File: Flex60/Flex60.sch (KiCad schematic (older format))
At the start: 128 parts, among them SW1 RESET, U1 ATmega32U4-AU, Y1 16MHz

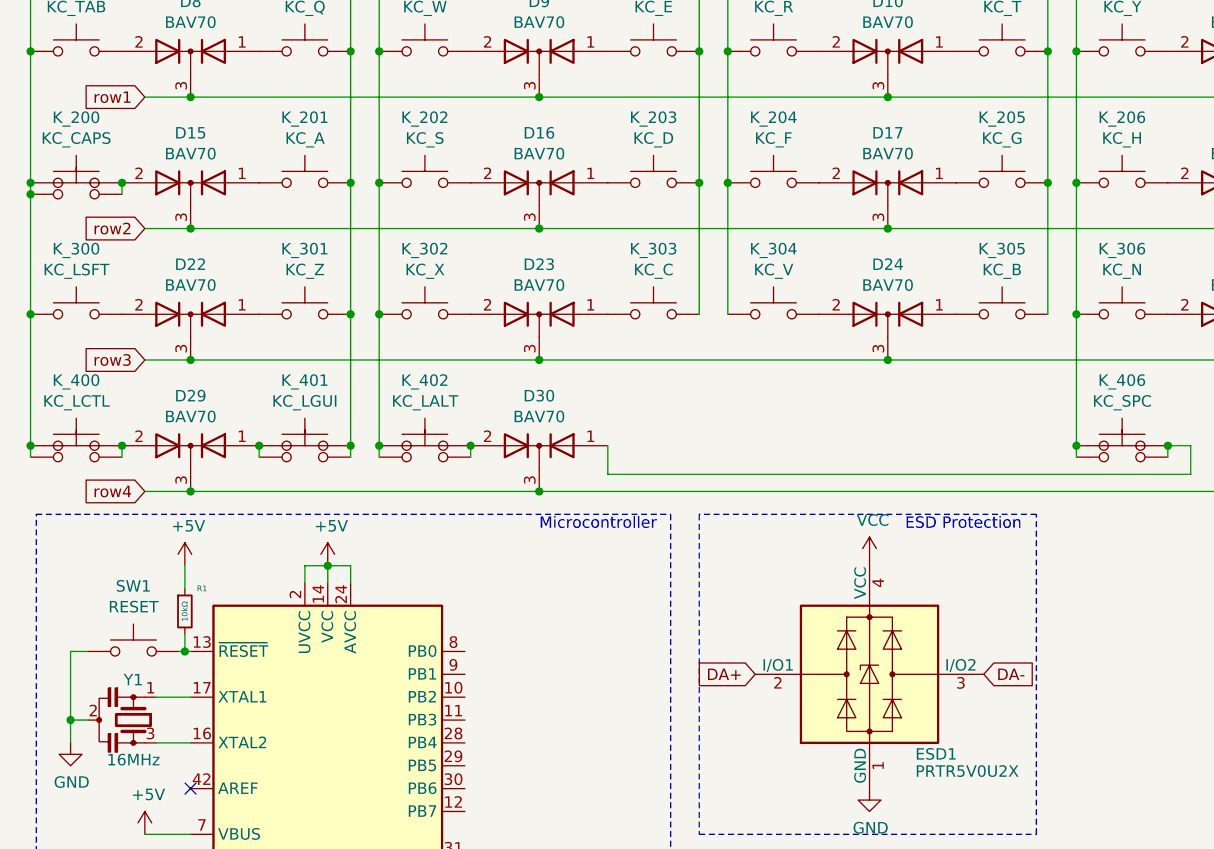
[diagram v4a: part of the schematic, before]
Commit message: MCU placement
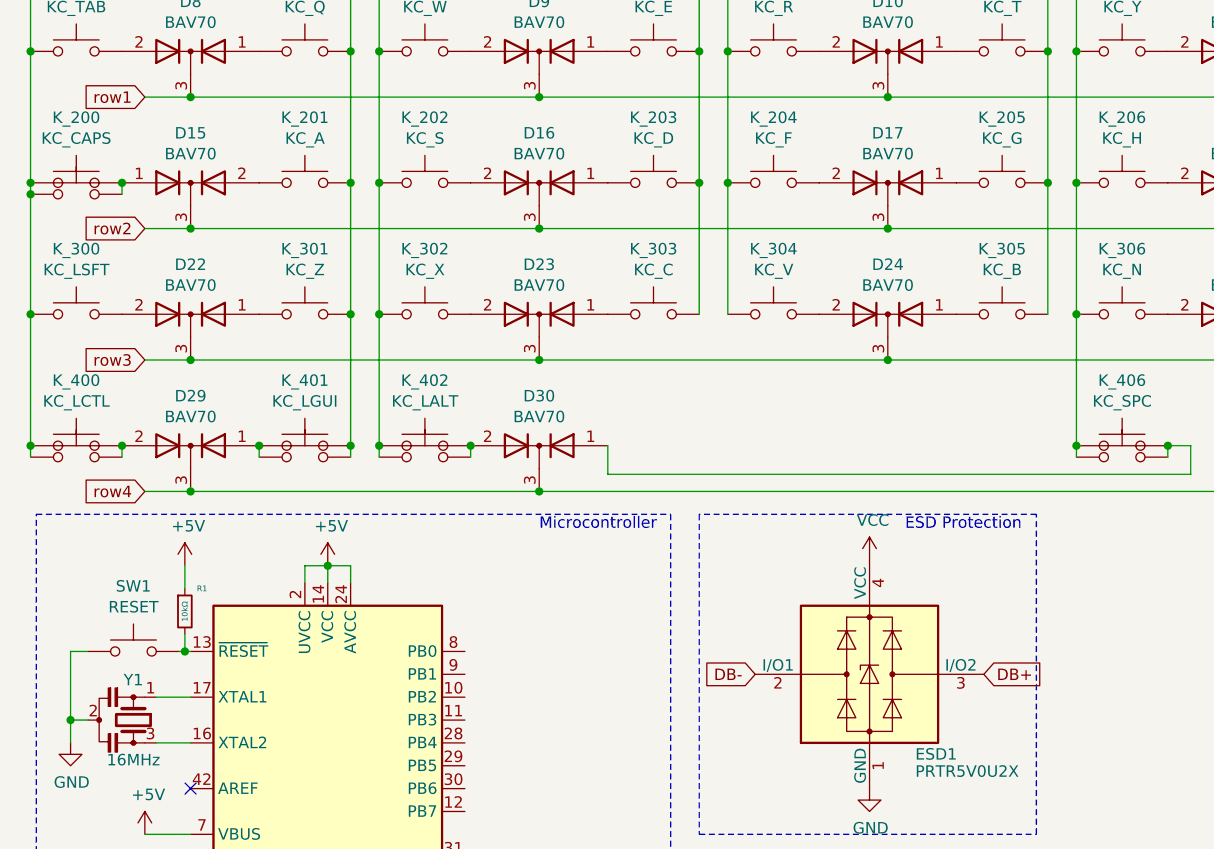
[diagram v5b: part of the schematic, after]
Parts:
- SW1: footprint Custom_Footprints:Tactile_Switch -> Custom_Footprints:RESET_PADS
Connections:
- net DA+: no longer ESD1.2 (I/O1)
- net DA-: no longer ESD1.3 (I/O2)
- net DB+: now also ESD1.3 (I/O2)
- net DB-: now also ESD1.2 (I/O1)
- net at K_200.2, K_200A1.2: now also D15.1 (A); no longer D15.2 (A)
- net at K_201.2: now also D15.2 (A); no longer D15.1 (A)
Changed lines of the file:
@@
 F 3 "https://assets.nexperia.com/documents/data-sheet/BAV70_SER.pdf" H 1275 1975 50  0001 C CNN
 	1    1275 1975
-	-1   0    0    -1
+	1    0    0    -1
 $EndComp
 $Comp
@@
 F 0 "SW1" H 1025 4310 50  0000 C CNN
 F 1 "RESET" H 1025 4219 50  0000 C CNN
-F 2 "Custom_Footprints:Tactile_Switch" H 1025 4225 50  0001 C CNN
+F 2 "Custom_Footprints:RESET_PADS" H 1025 4225 50  0001 C CNN
 F 3 "~" H 1025 4225 50  0001 C CNN
 	1    1025 4025
@@
 ESD Protection
 Text GLabel 3745 4125 0    50   Input ~ 0
-DA+
+DB-
 Text GLabel 4745 4125 2    50   Input ~ 0
-DA-
+DB+
 $EndSCHEMATC

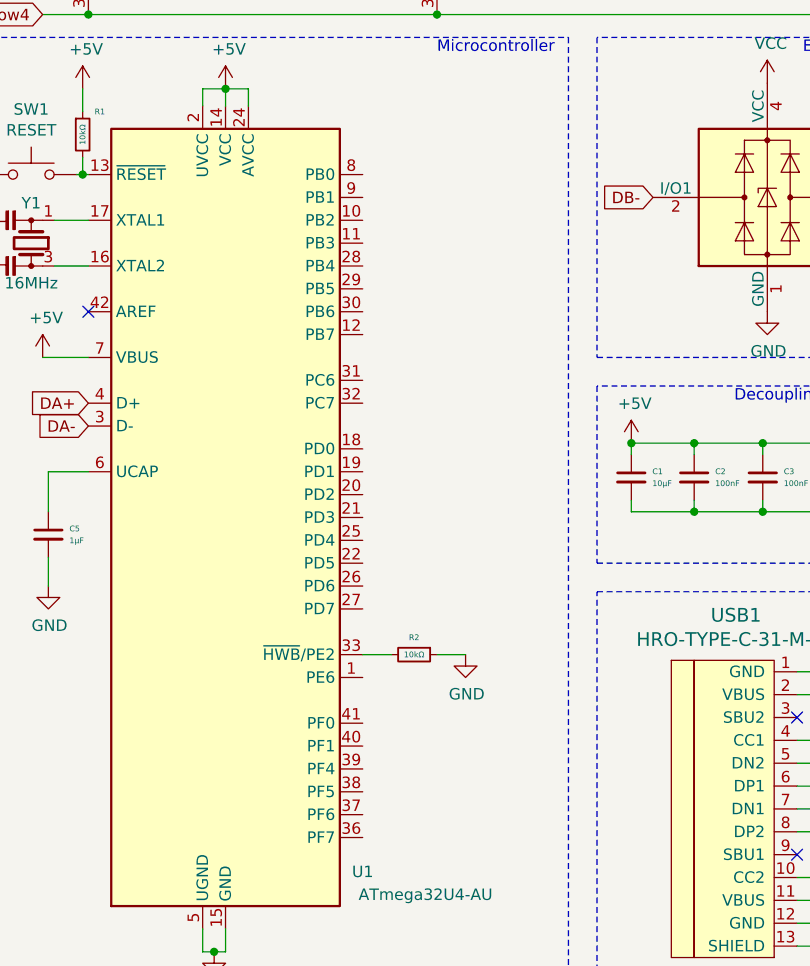
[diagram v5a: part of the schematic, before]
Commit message: Route Matrix
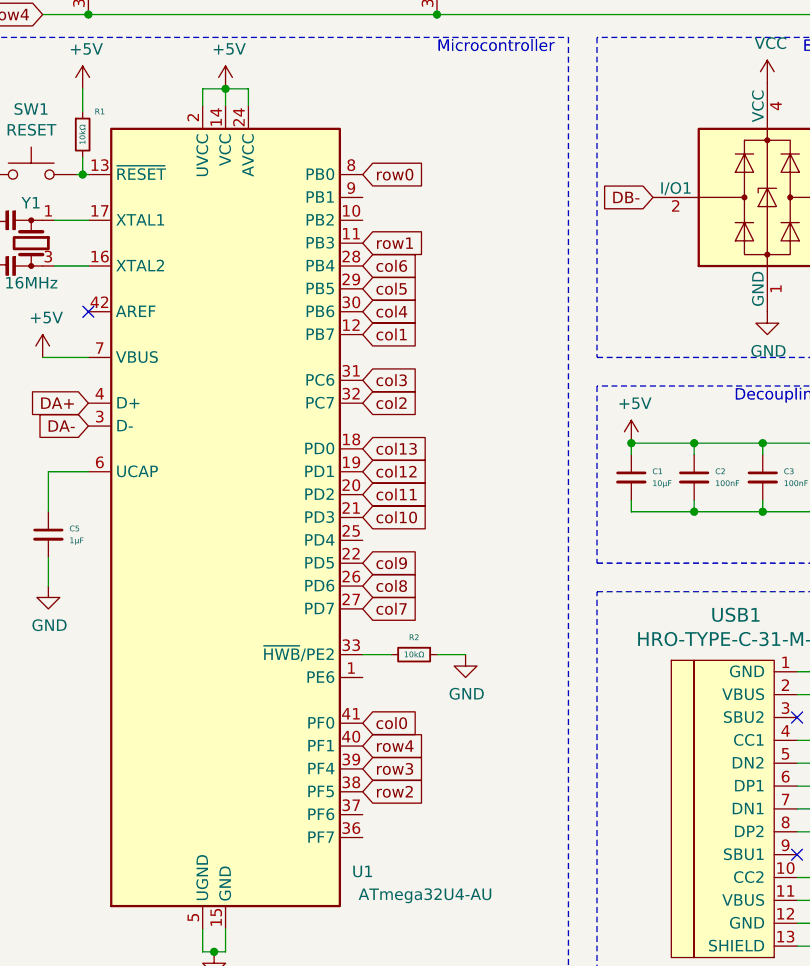
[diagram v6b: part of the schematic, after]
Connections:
- net col0: now also U1.41 (PF0)
- net col1: now also U1.12 (PB7)
- net col10: now also U1.21 (PD3)
- net col11: now also U1.20 (PD2)
- net col12: now also U1.19 (PD1)
- net col13: now also U1.18 (PD0)
- net col2: now also U1.32 (PC7)
- net col3: now also U1.31 (PC6)
- net col4: now also U1.30 (PB6)
- net col5: now also U1.29 (PB5)
- net col6: now also U1.28 (PB4)
- net col7: now also U1.27 (PD7)
- net col8: now also U1.26 (PD6)
- net col9: now also U1.22 (PD5)
- net row0: now also U1.8 (PB0)
- net row1: now also U1.11 (PB3)
- net row2: now also U1.38 (PF5)
- net row3: now also U1.39 (PF4)
- net row4: now also U1.40 (PF1)
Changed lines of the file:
@@
 Text GLabel 4745 4125 2    50   Input ~ 0
 DB+
+Text GLabel 2475 4725 2    50   Input ~ 0
+col1
+Text GLabel 2475 6425 2    50   Input ~ 0
+col0
+Text GLabel 2475 4025 2    50   Input ~ 0
+row0
+Text GLabel 2475 4325 2    50   Input ~ 0
+row1
+Text GLabel 2475 6725 2    50   Input ~ 0
+row2
+Text GLabel 2475 6625 2    50   Input ~ 0
+row3
+Text GLabel 2475 6525 2    50   Input ~ 0
+row4
+Text GLabel 2475 5225 2    50   Input ~ 0
+col13
+Text GLabel 2475 5325 2    50   Input ~ 0
+col12
+Text GLabel 2475 5425 2    50   Input ~ 0
+col11
+Text GLabel 2475 5525 2    50   Input ~ 0
+col10
+Text GLabel 2475 5725 2    50   Input ~ 0
+col9
+Text GLabel 2475 5825 2    50   Input ~ 0
+col8
+Text GLabel 2475 5925 2    50   Input ~ 0
+col7
+Text GLabel 2475 4425 2    50   Input ~ 0
+col6
+Text GLabel 2475 4525 2    50   Input ~ 0
+col5
+Text GLabel 2475 4625 2    50   Input ~ 0
+col4
+Text GLabel 2475 4925 2    50   Input ~ 0
+col3
+Text GLabel 2475 5025 2    50   Input ~ 0
+col2
 $EndSCHEMATC
